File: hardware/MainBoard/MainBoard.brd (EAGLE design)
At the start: 90 x 56 mm, 265 parts, among them J1 CON-71741-2184-BOT, J2 CON-71741-2184-TOP, J3 CON-FTSH-105-01-L-DV-K, J4 CON-ZX62R-B-5P, J7 CON-RJ45-J0G-0007NL, J8 SWITCH-CJS-1200-1200, M1 MOUNT-HOLE3.3, M2 MOUNT-HOLE3.3, M3 MOUNT-HOLE3.3, M4 MOUNT-HOLE3.3, M5 FIDUCIAL1X2, M6 FIDUCIAL1X2, M7 FIDUCIAL1X2, M8 FIDUCIAL1X2, Q1 MMBT3904, SW1 SWITCH-ESWITCH-TL3340G, SW2 SWITCH-ESWITCH-TL3340G, U1 A2F500M3G-1FGG256, U2 MAX19706-T4877-4, U3 MAX19706-T4877-4, U4 USBLC6-2SC6, U5 FT232HL, U6 DP83848C-VBH48A, U7 93LC56BT-OT, U8 DS1818-10-SOT-23, X1 ECX-2236-200, X2 ECX-31B, X3 ASEM1-C, X5 ECX-42-120

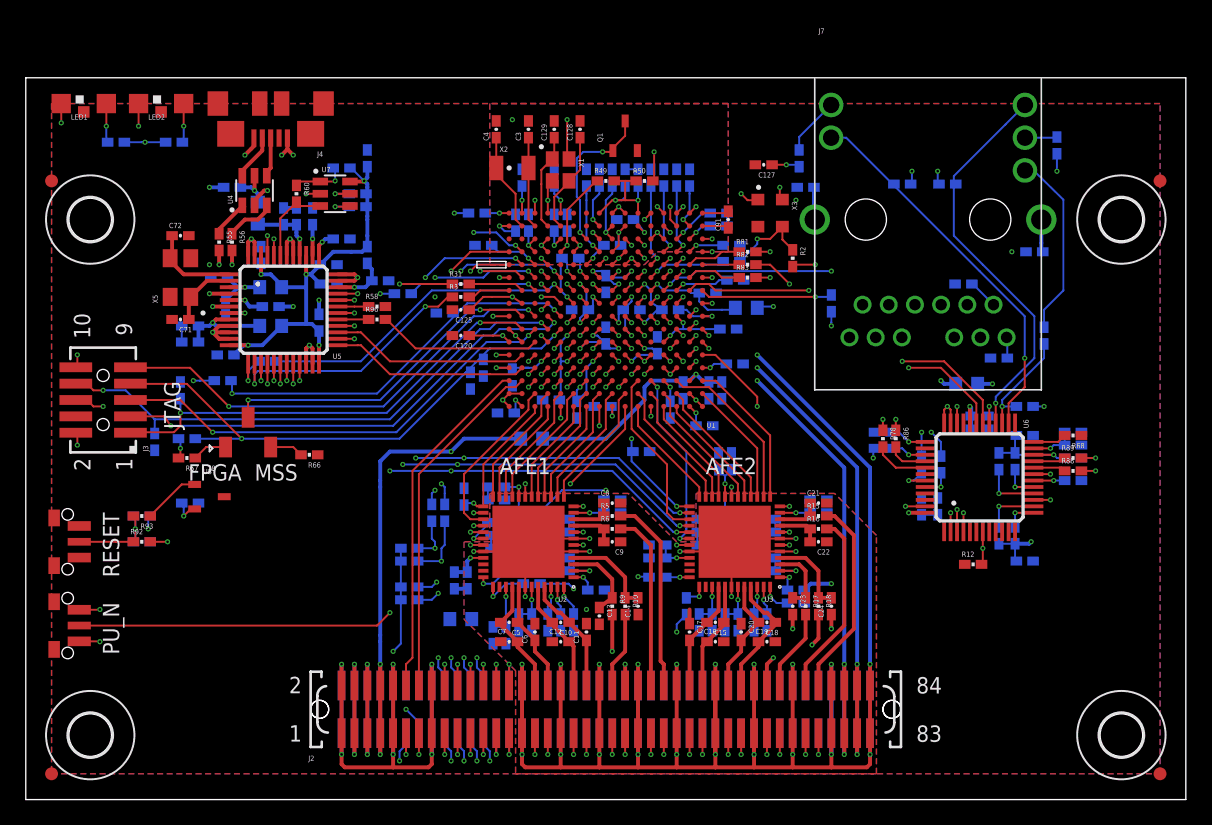
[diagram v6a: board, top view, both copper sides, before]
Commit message: Updating labels and JTAGSEL placement.
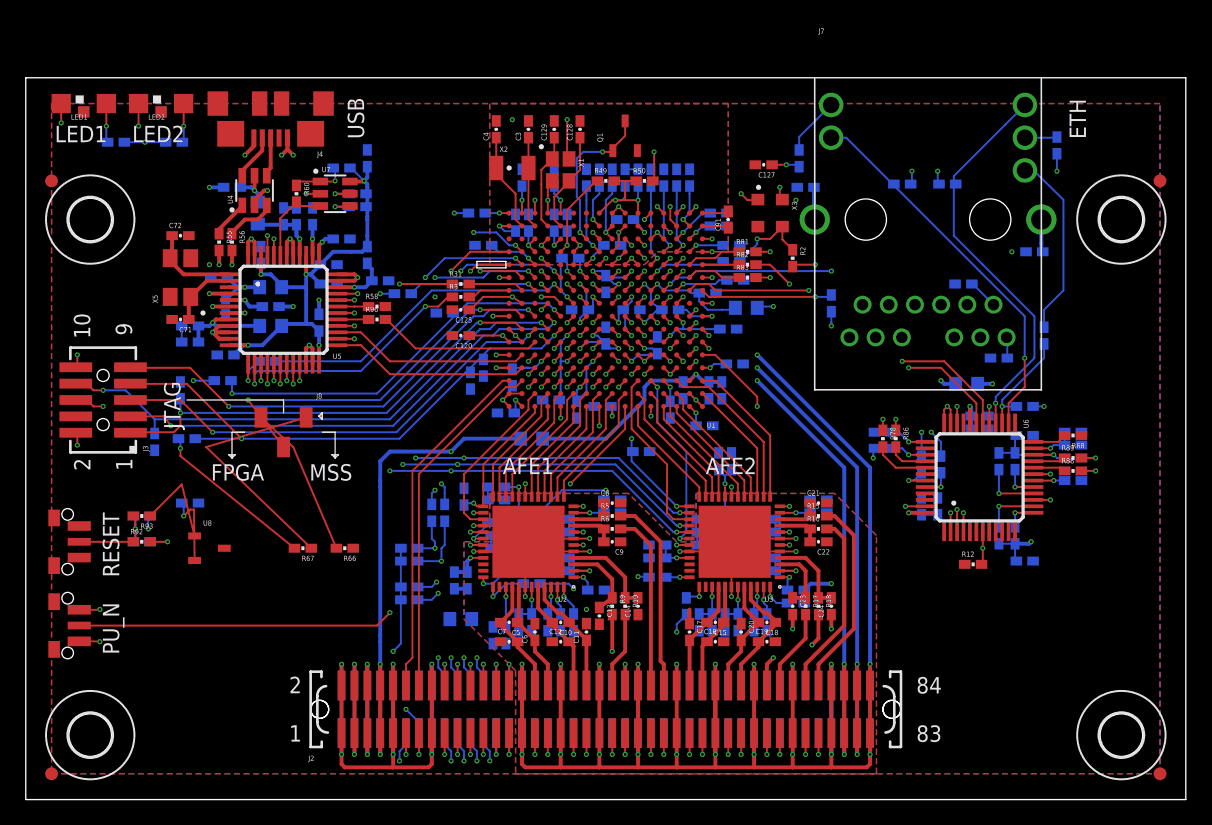
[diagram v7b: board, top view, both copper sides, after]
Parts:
- LOGO1: device Logo:LOGO-ISIS-10MM-PLACEHOLDER -> Logo:LOGO-ISIS-10MM-GOLD
- LOGO2: value LOGO-VANDERBILT-600MIL-10MM-PH -> LOGO-VANDERBILT-600MIL-10MM-AU; device Logo:LOGO-VANDERBILT-10MM-PLACEHOLDER -> Logo:LOGO-VANDERBILT-10MM-GOLD
- LOGO3: value LOGO-MARMOTE-600MIL-10MM-PH -> LOGO-MARMOTE-600MIL-10MM-AU; device Logo:LOGO-MARMOTE-10MM-PLACEHOLDER -> Logo:LOGO-MARMOTE-10MM-GOLD
- LOGO4: value LOGO-SMARTFUSION-600MIL-10MM-PH -> LOGO-SMARTFUSION-600MIL-10MM-AU; device Logo:LOGO-SMARTFUSION-10MM-PLACEHOLDER -> Logo:LOGO-SMARTFUSION-10MM-GOLD
- moved LOGO3 15.0 mm to (20.5, 58.5)
- moved R67 11.4 mm to (21.5, 19.5)
- moved LOGO4 8.06 mm to (33.5, 58.5)
- moved R66 7.75 mm to (24.8, 19.5)
- moved LOGO1 4.12 mm to (59.5, 58.5)
- moved U8 4.00 mm to (14.2, 19.5)
- moved J8 2.75 mm to (20.0, 28.5), turned to 180 degrees
- moved LOGO2 1.41 mm to (46.5, 58.5)
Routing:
- net FPGATAP: track 2.70 -> 19.4 mm
- net D3V3: track 133.9 -> 149.0 mm
- net MSSTAP: track 2.60 -> 11.9 mm
- net JTAGSEL: track 25.7 -> 28.9 mm
- net EXTIC-RST: track 4.46 -> 7.59 mm
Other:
- board text added: "ETH"
- board text added: "LED1"
- board text added: "LED2"
- board text added: "USB"

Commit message: Reset logic ripped up.
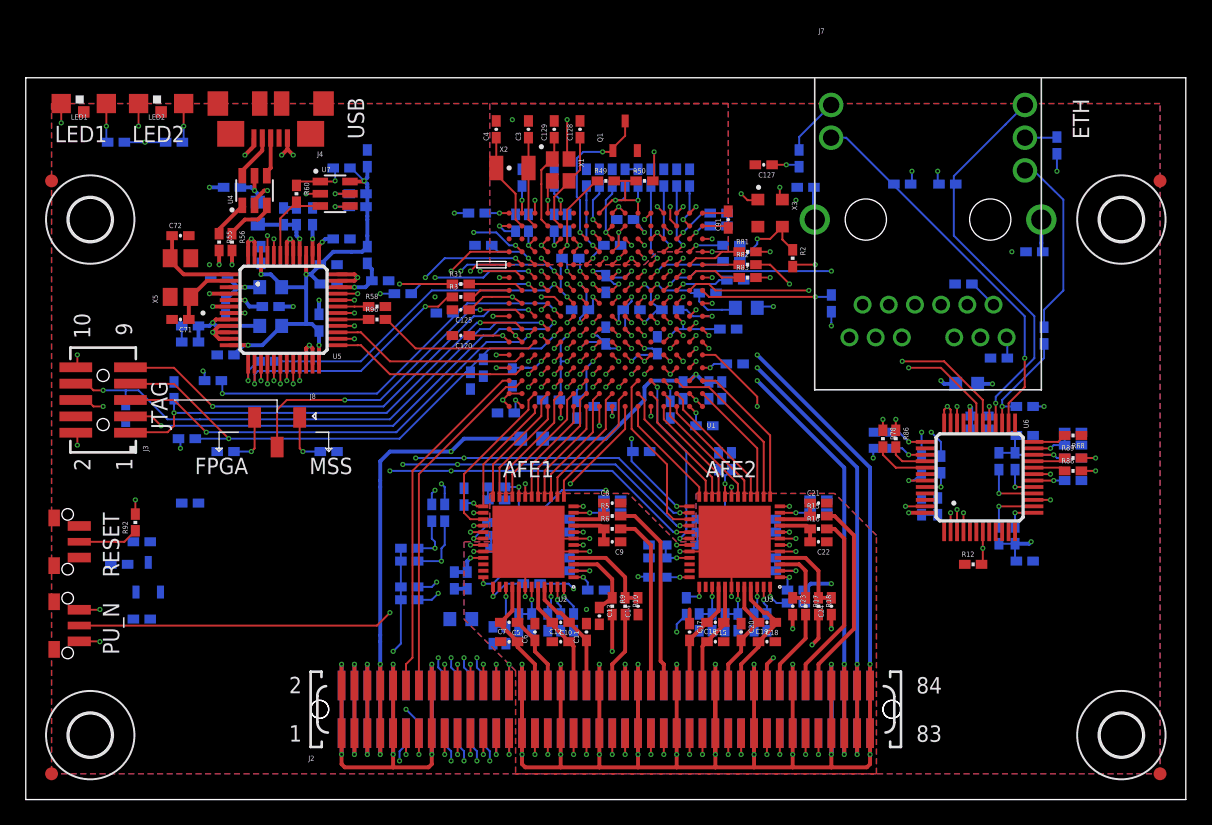
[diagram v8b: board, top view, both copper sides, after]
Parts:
- moved LOGO2 66.6 mm to (10.5, 2.50)
- moved LOGO1 56.9 mm to (69.5, 2.50)
- moved LOGO4 45.4 mm to (22.5, 14.5)
- moved LOGO3 45.1 mm to (10.5, 14.5)
- moved R66 11.9 mm to (15.5, 27.0), flipped to the bottom
- moved R91 8.00 mm to (9.00, 14.0)
- moved R67 7.76 mm to (23.5, 27.0), flipped to the bottom
- moved U8 5.26 mm to (9.50, 17.2), flipped to the bottom, turned to 90 degrees
- moved R93 4.14 mm to (7.25, 18.2), flipped to the bottom
- moved R64 3.18 mm to (7.75, 30.0)
- moved R92 1.58 mm to (8.50, 21.5), turned to 90 degrees
- moved R8 0.75 mm to (14.5, 32.5)
- moved J8 0.50 mm to (19.5, 28.5)
- moved R65 0.50 mm to (11.5, 31.8)
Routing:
- net D3V3: track 149.0 -> 129.1 mm, vias 46 -> 44
- net FPGATAP: track 19.4 -> 4.10 mm, vias 0 -> 1
- net MSSTAP: track 11.9 -> 4.10 mm, vias 0 -> 1
- net EXTIC-RST: track 7.59 -> 0.00 mm
- net !MSS_RESET: track 111.0 -> 106.9 mm
- net JTAGSEL: track 28.9 -> 25.3 mm
- net !MSS_RESET_PB: track 8.45 -> 4.95 mm, vias 1 -> 0
- net VPUMP: track 43.1 -> 42.1 mm
